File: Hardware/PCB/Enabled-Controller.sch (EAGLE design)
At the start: 14 parts, among them U1 ITSYBITSY

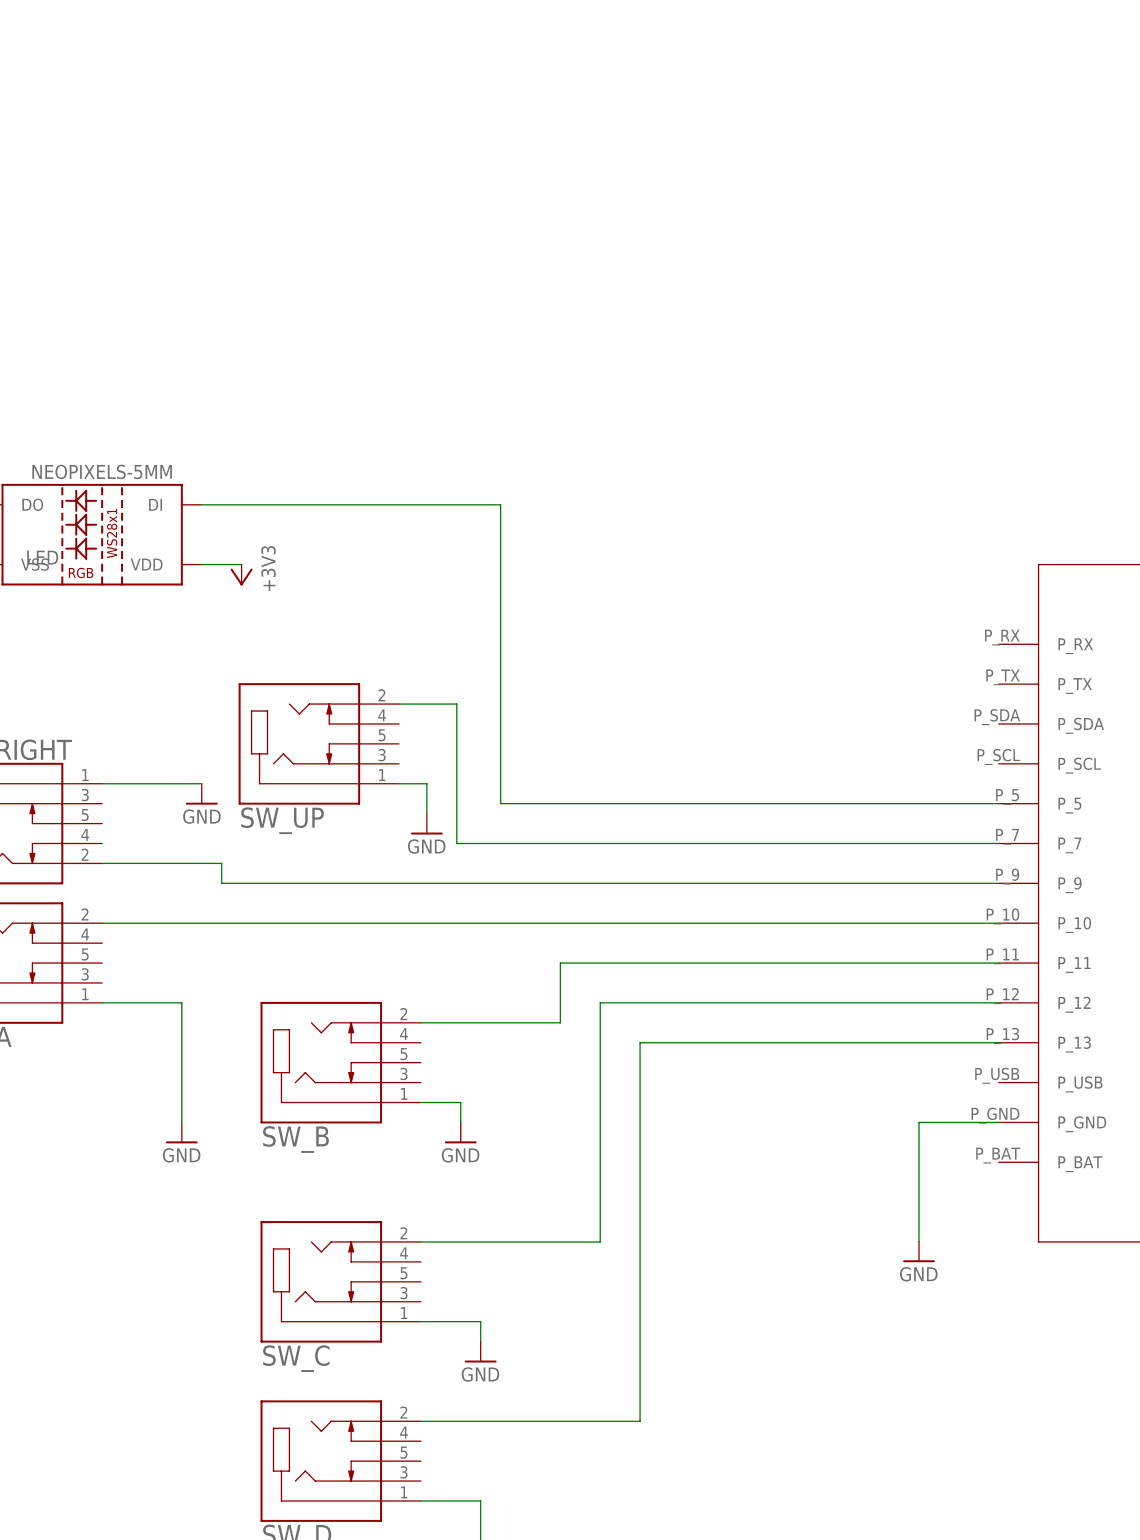
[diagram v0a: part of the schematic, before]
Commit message: Updated Eagle files
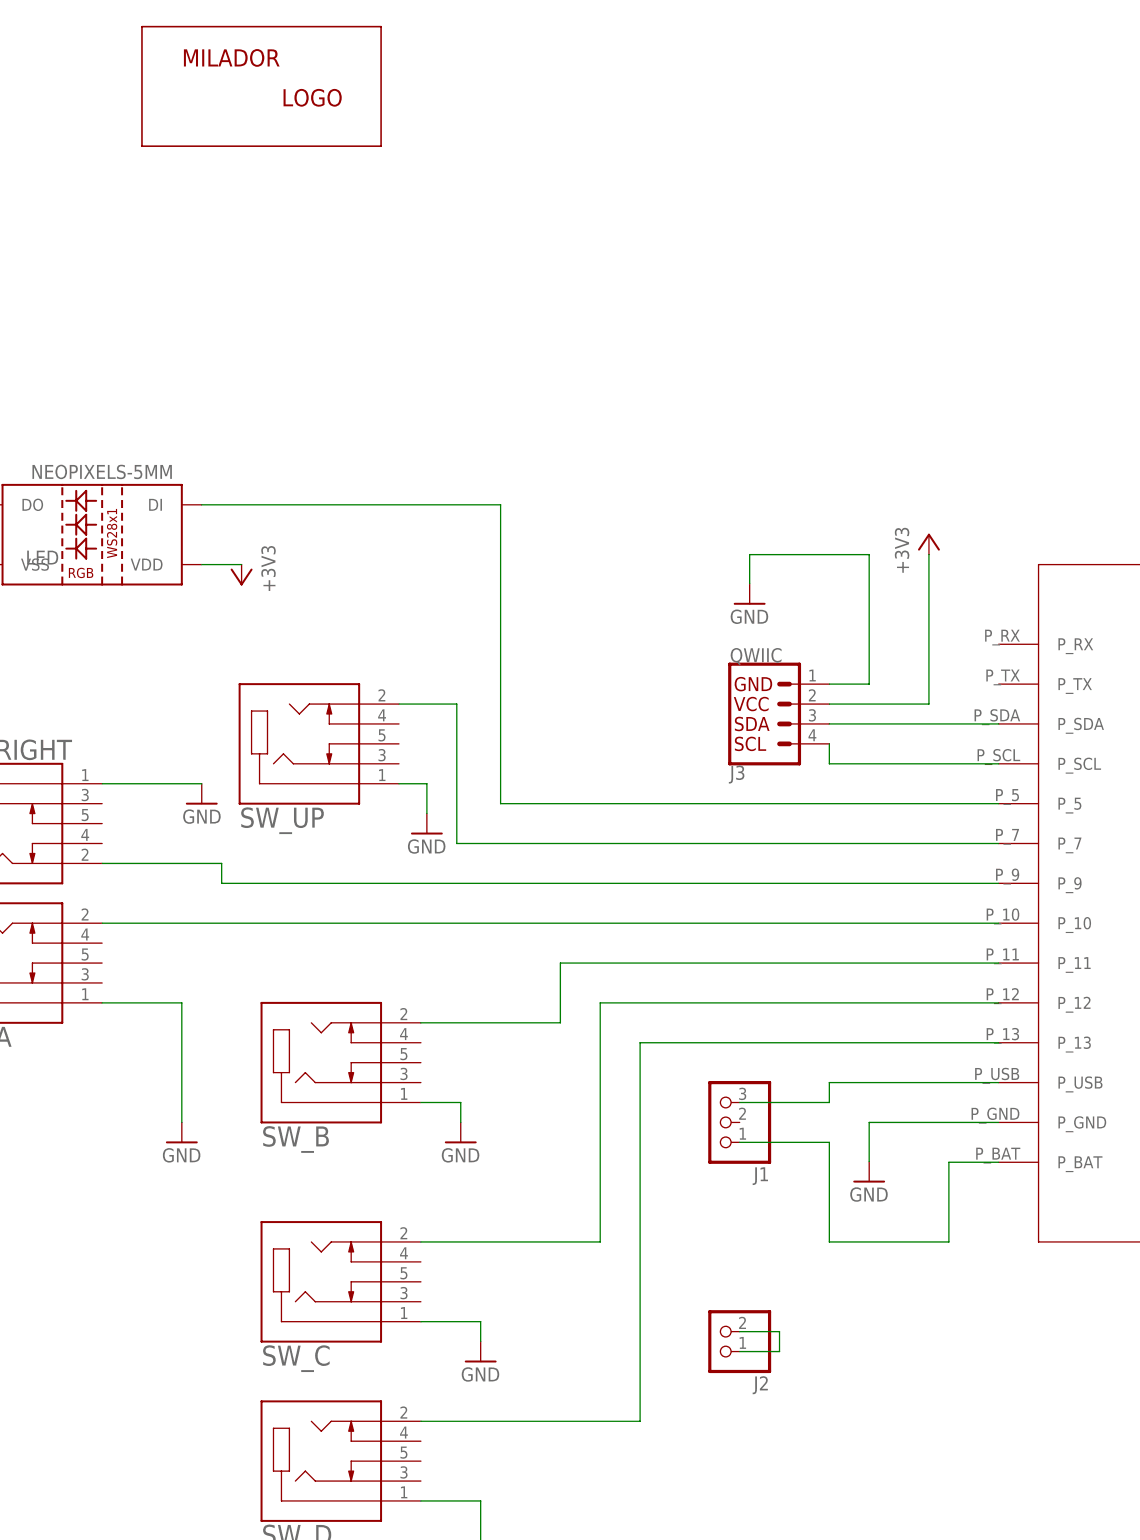
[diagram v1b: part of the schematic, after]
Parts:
- added J1: (no value), milador:HEADER_FEMALE-1X3-LONGER
- added J2: HEADER_FEMALE-1X2, milador:HEADER_FEMALE-1X2
- added J3: QWIIC, milador_SMD:QWIIC_CONNECTORSJS-1MM
- added U$1: MILADOR-LOGO-, milador:MILADOR-LOGO-
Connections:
- new net N$14: J3.4, U1.P_SCL
- new net N$15: J3.3, U1.P_SDA
- new net N$16: J1.3, U1.P_USB
- new net N$17: J1.1, U1.P_BAT
- new net N$18: J2.1, J2.2
- net +3V3: now also J3.2
- net GND: now also J3.1
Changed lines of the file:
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@@
 <?xml version="1.0" encoding="utf-8"?>
 <!DOCTYPE eagle SYSTEM "eagle.dtd">
-<eagle version="9.6.1">
+<eagle version="9.6.2">
 <drawing>
 <settings>
@@
 <layer number="154" name="FabDoc2" color="7" fill="1" visible="yes" active="yes"/>
 <layer number="155" name="FabDoc3" color="7" fill="1" visible="yes" active="yes"/>
+<layer number="160" name="O_Dim" color="7" fill="1" visible="yes" active="yes"/>
 <layer number="166" name="AntennaArea" color="7" fill="1" visible="yes" active="yes"/>
 <layer number="168" name="4mmHeightArea" color="7" fill="1" visible="yes" active="yes"/>
@@
 <part name="GND9" library="SparkFun-Aesthetics" deviceset="GND" device=""/>
 <part name="GND11" library="SparkFun-Aesthetics" deviceset="GND" device=""/>
+<part name="J3" library="milador_SMD" library_urn="urn:adsk.eagle:library:27847482" deviceset="QWIIC_CONNECTORS" device="JS-1MM" package3d_urn="urn:adsk.eagle:package:29222212/3" value="QWIIC"/>
+<part name="GND10" library="SparkFun-Aesthetics" deviceset="GND" device=""/>
+<part name="+3V3" library="supply1" library_urn="urn:adsk.eagle:library:371" deviceset="+3V3" device=""/>
+<part name="J1" library="milador" library_urn="urn:adsk.eagle:library:12595918" deviceset="HEADER_FEMALE-1X3-LONGER" device="" package3d_urn="urn:adsk.eagle:package:27250310/1"/>
+<part name="J2" library="milador" library_urn="urn:adsk.eagle:library:12595918" deviceset="HEADER_FEMALE-1X2" device="" package3d_urn="urn:adsk.eagle:package:27250301/1"/>
+<part name="U$1" library="milador" library_urn="urn:adsk.eagle:library:12595918" deviceset="MILADOR-LOGO-" device="" package3d_urn="urn:adsk.eagle:package:28431737/1"/>
 </parts>
 <sheets>
@@
 </plain>
 <instances>
-<instance part="GND2" gate="1" x="116.84" y="7.7" smashed="yes">
-<attribute name="VALUE" x="114.3" y="5.16" size="1.778" layer="96"/>
+<instance part="GND2" gate="1" x="110.49" y="17.86" smashed="yes">
+<attribute name="VALUE" x="107.95" y="15.32" size="1.778" layer="96"/>
 </instance>
 <instance part="FRAME1" gate="G$1" x="-48.26" y="-60.96" smashed="yes">
@@
 <attribute name="VALUE" x="51.562" y="59.69" size="1.778" layer="96"/>
 </instance>
+<instance part="J3" gate="G$1" x="97.79" y="78.74" smashed="yes" rot="MR180">
+<attribute name="VALUE" x="92.71" y="84.074" size="1.778" layer="96" font="vector" rot="MR180" align="top-left"/>
+<attribute name="NAME" x="92.71" y="70.866" size="1.778" layer="95" font="vector" rot="MR180"/>
+</instance>
+<instance part="GND10" gate="1" x="95.25" y="91.52" smashed="yes">
+<attribute name="VALUE" x="92.71" y="88.98" size="1.778" layer="96"/>
+</instance>
+<instance part="+3V3" gate="G$1" x="118.11" y="100.33" smashed="yes">
+<attribute name="VALUE" x="115.57" y="95.25" size="1.778" layer="96" rot="R90"/>
+</instance>
+<instance part="J1" gate="A" x="91.44" y="25.4" smashed="yes" rot="R180">
+<attribute name="NAME" x="97.79" y="19.685" size="1.778" layer="95" rot="R180"/>
+<attribute name="VALUE" x="97.79" y="33.02" size="1.778" layer="96" rot="R180"/>
+</instance>
+<instance part="J2" gate="G$1" x="91.44" y="-1.27" smashed="yes" rot="R180">
+<attribute name="NAME" x="97.79" y="-6.985" size="1.778" layer="95" rot="R180"/>
+</instance>
+<instance part="U$1" gate="G$1" x="33.02" y="157.48" smashed="yes"/>
 </instances>
 <busses>
@@
 <pinref part="GND2" gate="1" pin="GND"/>
 <pinref part="U1" gate="G$1" pin="P_GND"/>
-<wire x1="116.84" y1="10.24" x2="116.84" y2="25.4" width="0.1524" layer="91"/>
-<wire x1="116.84" y1="25.4" x2="127" y2="25.4" width="0.1524" layer="91"/>
+<wire x1="110.49" y1="20.4" x2="110.49" y2="25.4" width="0.1524" layer="91"/>
+<wire x1="110.49" y1="25.4" x2="127" y2="25.4" width="0.1524" layer="91"/>
 </segment>
 <segment>
@@
 <wire x1="54.102" y1="68.58" x2="50.546" y2="68.58" width="0.1524" layer="91"/>
 </segment>
+<segment>
+<pinref part="J3" gate="G$1" pin="1"/>
+<wire x1="105.41" y1="81.28" x2="110.49" y2="81.28" width="0.1524" layer="91"/>
+<wire x1="110.49" y1="81.28" x2="110.49" y2="97.79" width="0.1524" layer="91"/>
+<wire x1="110.49" y1="97.79" x2="95.25" y2="97.79" width="0.1524" layer="91"/>
+<pinref part="GND10" gate="1" pin="GND"/>
+<wire x1="95.25" y1="97.79" x2="95.25" y2="94.06" width="0.1524" layer="91"/>
+</segment>
 </net>
 <net name="+3V3" class="0">
@@
 <wire x1="208.28" y1="78.74" x2="205.74" y2="78.74" width="0.1524" layer="91"/>
 <wire x1="205.74" y1="78.74" x2="205.74" y2="81.28" width="0.1524" layer="91"/>
+</segment>
+<segment>
+<pinref part="J3" gate="G$1" pin="2"/>
+<pinref part="+3V3" gate="G$1" pin="+3V3"/>
+<wire x1="105.41" y1="78.74" x2="118.11" y2="78.74" width="0.1524" layer="91"/>
+<wire x1="118.11" y1="78.74" x2="118.11" y2="97.79" width="0.1524" layer="91"/>
 </segment>
 </net>
@@
 </segment>
 </net>
+<net name="N$14" class="0">
+<segment>
+<pinref part="U1" gate="G$1" pin="P_SCL"/>
+<wire x1="127" y1="71.12" x2="105.41" y2="71.12" width="0.1524" layer="91"/>
+<pinref part="J3" gate="G$1" pin="4"/>
+<wire x1="105.41" y1="71.12" x2="105.41" y2="73.66" width="0.1524" layer="91"/>
+</segment>
+</net>
+<net name="N$15" class="0">
+<segment>
+<pinref part="U1" gate="G$1" pin="P_SDA"/>
+<pinref part="J3" gate="G$1" pin="3"/>
+<wire x1="127" y1="76.2" x2="105.41" y2="76.2" width="0.1524" layer="91"/>
+</segment>
+</net>
+<net name="N$16" class="0">
+<segment>
+<pinref part="U1" gate="G$1" pin="P_USB"/>
+<wire x1="127" y1="30.48" x2="105.41" y2="30.48" width="0.1524" layer="91"/>
+<pinref part="J1" gate="A" pin="3"/>
+<wire x1="105.41" y1="30.48" x2="105.41" y2="27.94" width="0.1524" layer="91"/>
+<wire x1="105.41" y1="27.94" x2="93.98" y2="27.94" width="0.1524" layer="91"/>
+</segment>
+</net>
+<net name="N$17" class="0">
+<segment>
+<pinref part="J1" gate="A" pin="1"/>
+<wire x1="93.98" y1="22.86" x2="105.41" y2="22.86" width="0.1524" layer="91"/>
+<wire x1="105.41" y1="22.86" x2="105.41" y2="10.16" width="0.1524" layer="91"/>
+<wire x1="105.41" y1="10.16" x2="120.65" y2="10.16" width="0.1524" layer="91"/>
+<wire x1="120.65" y1="10.16" x2="120.65" y2="20.32" width="0.1524" layer="91"/>
+<pinref part="U1" gate="G$1" pin="P_BAT"/>
+<wire x1="120.65" y1="20.32" x2="127" y2="20.32" width="0.1524" layer="91"/>
+</segment>
+</net>
+<net name="N$18" class="0">
+<segment>
+<pinref part="J2" gate="G$1" pin="2"/>
+<wire x1="93.98" y1="-1.27" x2="99.06" y2="-1.27" width="0.1524" layer="91"/>
+<pinref part="J2" gate="G$1" pin="1"/>
+<wire x1="99.06" y1="-1.27" x2="99.06" y2="-3.81" width="0.1524" layer="91"/>
+<wire x1="99.06" y1="-3.81" x2="93.98" y2="-3.81" width="0.1524" layer="91"/>
+</segment>
+</net>

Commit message: Added updated PCB files
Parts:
- removed J2: HEADER_FEMALE-1X2, milador:HEADER_FEMALE-1X2
- renumbered U$1 to LABEL1
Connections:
- removed net N$18: J2.1, J2.2
- net GND: now also J1.2, SW_A.3, SW_B.3, SW_C.3, SW_D.3, SW_DOWN.3, SW_LEFT.3, SW_RIGHT.3, SW_UP.3
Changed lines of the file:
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@@
 <part name="+3V3" library="supply1" library_urn="urn:adsk.eagle:library:371" deviceset="+3V3" device=""/>
 <part name="J1" library="milador" library_urn="urn:adsk.eagle:library:12595918" deviceset="HEADER_FEMALE-1X3-LONGER" device="" package3d_urn="urn:adsk.eagle:package:27250310/1"/>
-<part name="J2" library="milador" library_urn="urn:adsk.eagle:library:12595918" deviceset="HEADER_FEMALE-1X2" device="" package3d_urn="urn:adsk.eagle:package:27250301/1"/>
-<part name="U$1" library="milador" library_urn="urn:adsk.eagle:library:12595918" deviceset="MILADOR-LOGO-" device="" package3d_urn="urn:adsk.eagle:package:28431737/1"/>
+<part name="LABEL1" library="milador" library_urn="urn:adsk.eagle:library:12595918" deviceset="MILADOR-LOGO-" device="" package3d_urn="urn:adsk.eagle:package:28431737/1"/>
 </parts>
 <sheets>
@@
 <attribute name="VALUE" x="97.79" y="33.02" size="1.778" layer="96" rot="R180"/>
 </instance>
-<instance part="J2" gate="G$1" x="91.44" y="-1.27" smashed="yes" rot="R180">
-<attribute name="NAME" x="97.79" y="-6.985" size="1.778" layer="95" rot="R180"/>
-</instance>
-<instance part="U$1" gate="G$1" x="33.02" y="157.48" smashed="yes"/>
+<instance part="LABEL1" gate="G$1" x="33.02" y="157.48" smashed="yes"/>
 </instances>
 <busses>
@@
 <wire x1="110.49" y1="20.4" x2="110.49" y2="25.4" width="0.1524" layer="91"/>
 <wire x1="110.49" y1="25.4" x2="127" y2="25.4" width="0.1524" layer="91"/>
+<pinref part="J1" gate="A" pin="2"/>
+<wire x1="93.98" y1="25.4" x2="110.49" y2="25.4" width="0.1524" layer="91"/>
+<junction x="110.49" y="25.4"/>
 </segment>
 <segment>
@@
 <wire x1="22.86" y1="25.4" x2="22.86" y2="40.64" width="0.1524" layer="91"/>
 <pinref part="SW_A" gate="G$1" pin="1"/>
-<wire x1="22.86" y1="40.64" x2="12.7" y2="40.64" width="0.1524" layer="91"/>
+<wire x1="22.86" y1="40.64" x2="15.24" y2="40.64" width="0.1524" layer="91"/>
+<pinref part="SW_A" gate="G$1" pin="3"/>
+<wire x1="15.24" y1="40.64" x2="12.7" y2="40.64" width="0.1524" layer="91"/>
+<wire x1="12.7" y1="43.18" x2="15.24" y2="43.18" width="0.1524" layer="91"/>
+<wire x1="15.24" y1="43.18" x2="15.24" y2="40.64" width="0.1524" layer="91"/>
+<junction x="15.24" y="40.64"/>
 </segment>
 <segment>
 <pinref part="SW_LEFT" gate="G$1" pin="1"/>
 <pinref part="GND13" gate="1" pin="GND"/>
-<wire x1="299.72" y1="63.5" x2="294.64" y2="63.5" width="0.1524" layer="91"/>
+<wire x1="299.72" y1="63.5" x2="297.18" y2="63.5" width="0.1524" layer="91"/>
+<pinref part="SW_LEFT" gate="G$1" pin="3"/>
+<wire x1="297.18" y1="63.5" x2="294.64" y2="63.5" width="0.1524" layer="91"/>
+<wire x1="299.72" y1="60.96" x2="297.18" y2="60.96" width="0.1524" layer="91"/>
+<wire x1="297.18" y1="60.96" x2="297.18" y2="63.5" width="0.1524" layer="91"/>
+<junction x="297.18" y="63.5"/>
 </segment>
 <segment>
@@
 <pinref part="SW_RIGHT" gate="G$1" pin="1"/>
 <pinref part="GND6" gate="1" pin="GND"/>
-<wire x1="12.7" y1="68.58" x2="25.4" y2="68.58" width="0.1524" layer="91"/>
+<wire x1="12.7" y1="68.58" x2="16.51" y2="68.58" width="0.1524" layer="91"/>
+<pinref part="SW_RIGHT" gate="G$1" pin="3"/>
+<wire x1="16.51" y1="68.58" x2="25.4" y2="68.58" width="0.1524" layer="91"/>
+<wire x1="12.7" y1="66.04" x2="16.51" y2="66.04" width="0.1524" layer="91"/>
+<wire x1="16.51" y1="66.04" x2="16.51" y2="68.58" width="0.1524" layer="91"/>
+<junction x="16.51" y="68.58"/>
 </segment>
 <segment>
 <pinref part="SW_DOWN" gate="G$1" pin="1"/>
 <pinref part="GND5" gate="1" pin="GND"/>
-<wire x1="299.72" y1="88.9" x2="287.02" y2="88.9" width="0.1524" layer="91"/>
+<wire x1="299.72" y1="88.9" x2="297.18" y2="88.9" width="0.1524" layer="91"/>
+<pinref part="SW_DOWN" gate="G$1" pin="3"/>
+<wire x1="297.18" y1="88.9" x2="287.02" y2="88.9" width="0.1524" layer="91"/>
+<wire x1="299.72" y1="86.36" x2="297.18" y2="86.36" width="0.1524" layer="91"/>
+<wire x1="297.18" y1="86.36" x2="297.18" y2="88.9" width="0.1524" layer="91"/>
+<junction x="297.18" y="88.9"/>
 </segment>
 <segment>
 <pinref part="SW_B" gate="G$1" pin="1"/>
 <pinref part="GND7" gate="1" pin="GND"/>
-<wire x1="53.34" y1="27.94" x2="58.42" y2="27.94" width="0.1524" layer="91"/>
+<wire x1="53.34" y1="27.94" x2="55.88" y2="27.94" width="0.1524" layer="91"/>
+<wire x1="55.88" y1="27.94" x2="58.42" y2="27.94" width="0.1524" layer="91"/>
 <wire x1="58.42" y1="27.94" x2="58.42" y2="25.4" width="0.1524" layer="91"/>
+<pinref part="SW_B" gate="G$1" pin="3"/>
+<wire x1="53.34" y1="30.48" x2="55.88" y2="30.48" width="0.1524" layer="91"/>
+<wire x1="55.88" y1="30.48" x2="55.88" y2="27.94" width="0.1524" layer="91"/>
+<junction x="55.88" y="27.94"/>
 </segment>
 <segment>
 <pinref part="SW_C" gate="G$1" pin="1"/>
 <pinref part="GND8" gate="1" pin="GND"/>
-<wire x1="53.34" y1="0" x2="60.96" y2="0" width="0.1524" layer="91"/>
+<wire x1="53.34" y1="0" x2="55.88" y2="0" width="0.1524" layer="91"/>
+<wire x1="55.88" y1="0" x2="60.96" y2="0" width="0.1524" layer="91"/>
 <wire x1="60.96" y1="0" x2="60.96" y2="-2.54" width="0.1524" layer="91"/>
+<pinref part="SW_C" gate="G$1" pin="3"/>
+<wire x1="53.34" y1="2.54" x2="55.88" y2="2.54" width="0.1524" layer="91"/>
+<wire x1="55.88" y1="2.54" x2="55.88" y2="0" width="0.1524" layer="91"/>
+<junction x="55.88" y="0"/>
 </segment>
 <segment>
 <pinref part="SW_D" gate="G$1" pin="1"/>
 <pinref part="GND9" gate="1" pin="GND"/>
-<wire x1="53.34" y1="-22.86" x2="60.96" y2="-22.86" width="0.1524" layer="91"/>
+<wire x1="53.34" y1="-22.86" x2="55.88" y2="-22.86" width="0.1524" layer="91"/>
+<wire x1="55.88" y1="-22.86" x2="60.96" y2="-22.86" width="0.1524" layer="91"/>
 <wire x1="60.96" y1="-22.86" x2="60.96" y2="-27.94" width="0.1524" layer="91"/>
+<pinref part="SW_D" gate="G$1" pin="3"/>
+<wire x1="53.34" y1="-20.32" x2="55.88" y2="-20.32" width="0.1524" layer="91"/>
+<wire x1="55.88" y1="-20.32" x2="55.88" y2="-22.86" width="0.1524" layer="91"/>
+<junction x="55.88" y="-22.86"/>
 </segment>
 <segment>
@@
 <pinref part="SW_UP" gate="G$1" pin="1"/>
 <wire x1="54.102" y1="64.77" x2="54.102" y2="68.58" width="0.1524" layer="91"/>
-<wire x1="54.102" y1="68.58" x2="50.546" y2="68.58" width="0.1524" layer="91"/>
+<wire x1="54.102" y1="68.58" x2="52.07" y2="68.58" width="0.1524" layer="91"/>
+<pinref part="SW_UP" gate="G$1" pin="3"/>
+<wire x1="52.07" y1="68.58" x2="50.546" y2="68.58" width="0.1524" layer="91"/>
+<wire x1="50.546" y1="71.12" x2="52.07" y2="71.12" width="0.1524" layer="91"/>
+<wire x1="52.07" y1="71.12" x2="52.07" y2="68.58" width="0.1524" layer="91"/>
+<junction x="52.07" y="68.58"/>
 </segment>
 <segment>
@@
 </segment>
 </net>
-<net name="N$18" class="0">
-<segment>
-<pinref part="J2" gate="G$1" pin="2"/>
-<wire x1="93.98" y1="-1.27" x2="99.06" y2="-1.27" width="0.1524" layer="91"/>
-<pinref part="J2" gate="G$1" pin="1"/>
-<wire x1="99.06" y1="-1.27" x2="99.06" y2="-3.81" width="0.1524" layer="91"/>
-<wire x1="99.06" y1="-3.81" x2="93.98" y2="-3.81" width="0.1524" layer="91"/>
-</segment>
-</net>
